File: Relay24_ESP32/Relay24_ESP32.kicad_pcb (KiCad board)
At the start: 2 copper layers, 210 x 120 mm, 163 parts, among them J1 Section 1, J10 Section 10, J11 Section 11, J12 Section 12, J13 Section 13, J14 Section 14, J15 Section 15, J16 Section 16, J17 Section 17, J18 Section 18, J19 Section 19, J2 Section 2, J20 Section 20, J21 Section 21, J22 Section 22, J23 Section 23, J24 Section 24, J25 12V IN, J26 12V ACT A (left), J27 12V ACT A (right), J28 12V ACT B (left), J29 12V ACT B (right), J3 Section 3, J30 DevKitC J2 (3V3..5V), J31 DevKitC J3 (GND..CLK), J32 HR911105A, J33 I2C, J34 Analog, J4 Section 4, J5 Section 5, J6 Section 6, J7 Section 7, J8 Section 8, J9 Section 9, K1 HF115F/012-2ZS4, K10 HF115F/012-2ZS4, K11 HF115F/012-2ZS4, K12 HF115F/012-2ZS4, K13 HF115F/012-2ZS4, K14 HF115F/012-2ZS4, K15 HF115F/012-2ZS4, K16 HF115F/012-2ZS4, K17 HF115F/012-2ZS4, K18 HF115F/012-2ZS4, K19 HF115F/012-2ZS4, K2 HF115F/012-2ZS4, K20 HF115F/012-2ZS4, K21 HF115F/012-2ZS4, K22 HF115F/012-2ZS4, K23 HF115F/012-2ZS4, K24 HF115F/012-2ZS4, K3 HF115F/012-2ZS4, K4 HF115F/012-2ZS4, K5 HF115F/012-2ZS4, K6 HF115F/012-2ZS4, K7 HF115F/012-2ZS4, K8 HF115F/012-2ZS4, K9 HF115F/012-2ZS4, U1 74HC595, U2 74HC595, U3 74HC595, U4 ULN2803A, U5 ULN2803A, U6 ULN2803A, U7 LM2596S-5.0, U8 AMS1117-3.3, U9 LAN8720A

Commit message: Relay24_ESP32: replace the LAN8720A with an RTL8201F (Economic PCBA)
JLCPCB assembles the LAN8720A (C45223) only on its Standard service,
so the Ethernet PHY is now a Realtek RTL8201F-VB-CG (C45044, QFN-32),
which is on the Economic service.

- RTL8201F runs on a 25 MHz crystal (Y1, C9006, 2x 18 pF C1647) and
  sends the 50 MHz RMII reference clock out of TXC through R30 (33 ohm)
  to GPIO0 (ETH_CLOCK_GPIO0_IN); GPIO17 is free again.
- Straps: RXDV pulled up (RMII), LED0/LED1 pulled down (PHY address 0,
  active-high LEDs). D30 shows a 10 Mbit link, D31 a 100 Mbit link.
- RSET 2.49k (C136931), PHYRSTB held low by R33 until GPIO33 is set.
- MDI pair 0 to RJ45 pins 1-2 and pair 1 to pins 3-6 (standard wiring),
  49.9 ohm terminations to 3V3 kept; new fan-out and pre-route for the
  QFN in make_pcb.py; custom schematic symbol in make_sch.py.
- router.py: the flood fill that finds existing copper of a net is now
  8-connected, so a diagonal fixed track is one piece of copper and the
  router no longer adds a wide stub next to it (clearance violation).
- make_pcb.py: RELAY24_FIXED_ONLY=1 builds only the hand-placed copper
  and runs the DRC, for quick checks.
- README, schematic, board, Gerber, BOM, CPL and views regenerated.
  Router failures 0, DRC 0 errors / 0 unconnected. Nothing built yet.

Co-Authored-By: Claude Fable 5.1 <noreply@anthropic.com>
Claude-Session: https://claude.ai/code/session_01VKEBDGHaGvWUQ7R6BJeKCx
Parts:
- removed R37: 10k, R_0603_1608Metric
- added C38: 10uF, C_0805_2012Metric, F.Cu at (55.5, 65.5)
- added Y1: 25MHz, Crystal_SMD_3225-4Pin_3.2x2.5mm, F.Cu at (68.9, 68.0)
- C34: value 1uF -> 18pF
- C35: value 10uF -> 18pF; footprint C_0805_2012Metric -> C_0603_1608Metric
- R31: value 12.1k 1% -> 2.49k 1%
- R32, R35, R36: value 10k -> 4.7k
- U9: value LAN8720A -> RTL8201F; footprint VQFN-24-1EP_4x4mm_P0.5mm_EP2.5x2.5mm_ThermalVias -> QFN-32-1EP_5x5mm_P0.5mm_EP3.45x3.45mm_ThermalVias
- moved R34 17.7 mm to (58.8, 55.3), turned to 90 degrees
- moved C35 16.5 mm to (70.8, 71.7), turned to -90 degrees
- moved R35 14.1 mm to (69.9, 56.4), turned to 90 degrees
- moved C31 13.3 mm to (71.4, 57.3), turned to 90 degrees
- moved R33 12.3 mm to (60.8, 55.3), turned to 90 degrees
- moved R43 12.0 mm to (63.4, 68.4), turned to -90 degrees
- moved R31 11.9 mm to (71.9, 63.3), turned to -90 degrees
- moved D31 7.87 mm to (63.4, 65.4), turned to 90 degrees
- moved R30 7.09 mm to (64.8, 55.3), turned to 90 degrees
- moved C32 6.48 mm to (73.5, 63.3), turned to -90 degrees
- moved C34 6.33 mm to (66.3, 68.3)
- moved R32 5.85 mm to (61.1, 63.9), turned to 0 degrees
- moved C30 5.02 mm to (66.4, 55.3), turned to 90 degrees
- moved R36 3.52 mm to (61.1, 65.6), turned to 0 degrees
- moved D30 2.70 mm to (61.1, 62.1)
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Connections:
- net LED_LNK_K renamed LED0_K
- C32 pad 1: +3V3 -> AVDD10
- C33 pad 1: VDDCR -> DVDD10
- C34 pad 1: VDDCR -> XTAL1
- C35 pad 1: +3V3 -> XTAL2
- D30 pad 2: LED_LNK -> PHY_LED0
- D31 pad 1: LED_SPD -> LED1_K
- D31 pad 2: LED_SPD_A -> PHY_LED1
- J31 pad 11: ETH_CLK -> (no net)
- J31 pad 14: (no net) -> ETH_CLK
- J32 pad 1: TXN -> MDI0P
- J32 pad 2: TXP -> MDI0N
- J32 pad 3: RXN -> MDI1P
- J32 pad 6: RXP -> MDI1N
- R30 pad 1: ETH_CLK -> ETH_REFCLK
- R30 pad 2: ETH_CLKIN -> ETH_CLK
- R31 pad 1: RBIAS -> RSET
- R32 pad 1: PHYAD0 -> GND
- R32 pad 2: GND -> PHY_LED0
- R35 pad 1: RMII_RXD0 -> PHY_RXDV
- R36 pad 1: RMII_RXD1 -> GND
- R36 pad 2: +3V3 -> PHY_LED1
- R38 pad 1: TXP -> MDI0N
- R39 pad 1: TXN -> MDI0P
- R40 pad 1: RXP -> MDI1N
- R41 pad 1: RXN -> MDI1P
- R43 pad 1: +3V3 -> LED1_K
- R43 pad 2: LED_SPD_A -> GND
- U9 pad 1: +3V3 -> RSET
- U9 pad 10: PHYAD0 -> RMII_RXD1
- U9 pad 11: RMII_CRS_DV -> (no net)
- U9 pad 12: RMII_MDIO -> (no net)
- U9 pad 13: RMII_MDC -> (no net)
- U9 pad 14: (no net) -> +3V3
- U9 pad 15: ETH_RST -> ETH_REFCLK
- U9 pad 16: RMII_TXEN -> RMII_TXD0
- U9 pad 17: RMII_TXD0 -> RMII_TXD1
- U9 pad 18: RMII_TXD1 -> (no net)
- U9 pad 19: +3V3 -> (no net)
- U9 pad 2: LED_SPD -> AVDD10
- U9 pad 20: TXN -> RMII_TXEN
- U9 pad 21: TXP -> ETH_RST
- U9 pad 22: RXN -> RMII_MDC
- U9 pad 23: RXP -> RMII_MDIO
- U9 pad 24: RBIAS -> PHY_LED0
- U9 pad 25: GND -> PHY_LED1
- U9 pad 3: LED_LNK -> MDI0P
- U9 pad 4: (no net) -> MDI0N
- U9 pad 5: ETH_CLKIN -> MDI1P
- U9 pad 6: VDDCR -> MDI1N
- U9 pad 7: RMII_RXD1 -> +3V3
- U9 pad 8: RMII_RXD0 -> PHY_RXDV
- U9 pad 9: +3V3 -> RMII_RXD0
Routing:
- net TXN: track 140.9 -> 0.00 mm, vias 1 -> 0
- net RXP: track 138.1 -> 0.00 mm, vias 1 -> 0
- net RXN: track 137.6 -> 0.00 mm, vias 1 -> 0
- net TXP: track 136.5 -> 0.00 mm, vias 1 -> 0
- net MDI0P: track 0.00 -> 131.4 mm, vias 0 -> 1
- net MDI1N: track 0.00 -> 128.1 mm, vias 0 -> 1
- net MDI1P: track 0.00 -> 126.6 mm, vias 0 -> 1
- net MDI0N: track 0.00 -> 126.0 mm, vias 0 -> 1
- net I2C_SDA: track 72.1 -> 111.8 mm, vias 1 -> 3
- net SR_Q1: track 117.8 -> 78.3 mm, vias 6 -> 2
- net GND: track 414.7 -> 452.0 mm, vias 49 -> 51
- net SR_SRCLK: track 242.8 -> 209.7 mm
- net SR_OE: track 258.7 -> 281.7 mm, vias 12 -> 9
- net ETH_CLK: track 44.1 -> 64.8 mm
- net SR_RCLK: track 200.7 -> 182.8 mm, vias 6 -> 8
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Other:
- board text added: "100M"
- board text added: "10M"
- board text removed: "LNK"
- board text removed: "SPD"

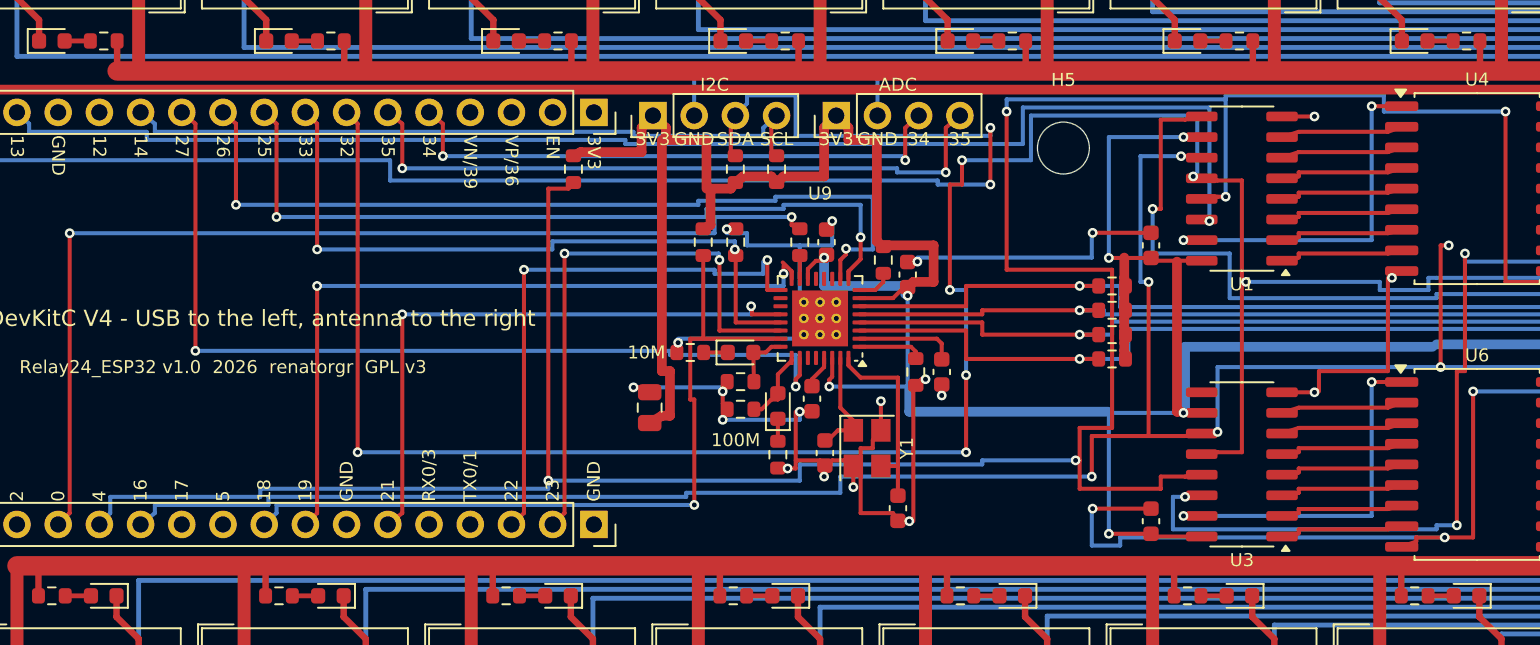
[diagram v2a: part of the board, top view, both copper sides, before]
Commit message: Relay24_ESP32: use a 5032 two-pin crystal that JLCPCB assembles normally
JLCPCB flags the 3225 four-pin crystal (C9006) as "Assembly Difficulty:
High" and warned that it may cost extra. Y1 is now the YXC X503225MSB2GI
(C112569, 25 MHz, 5.0 x 3.2 mm, two pins, CL 20 pF), which carries no
such flag.

- Load capacitors C34/C35 go from 18 pF to 33 pF (C1663, basic part)
  to match the 20 pF load capacitance.
- The crystal sits below the PHY, XTAL1 straight down from pin 31,
  XTAL2 from pin 32, each load capacitor right under its pad; the
  ground stubs and vias of the old crystal are gone.
- Schematic, board, Gerber, BOM, CPL, views and README regenerated.
  Router failures 0, DRC 0 errors / 0 unconnected.

Co-Authored-By: Claude Opus 5.5 <noreply@anthropic.com>
Claude-Session: https://claude.ai/code/session_01VKEBDGHaGvWUQ7R6BJeKCx
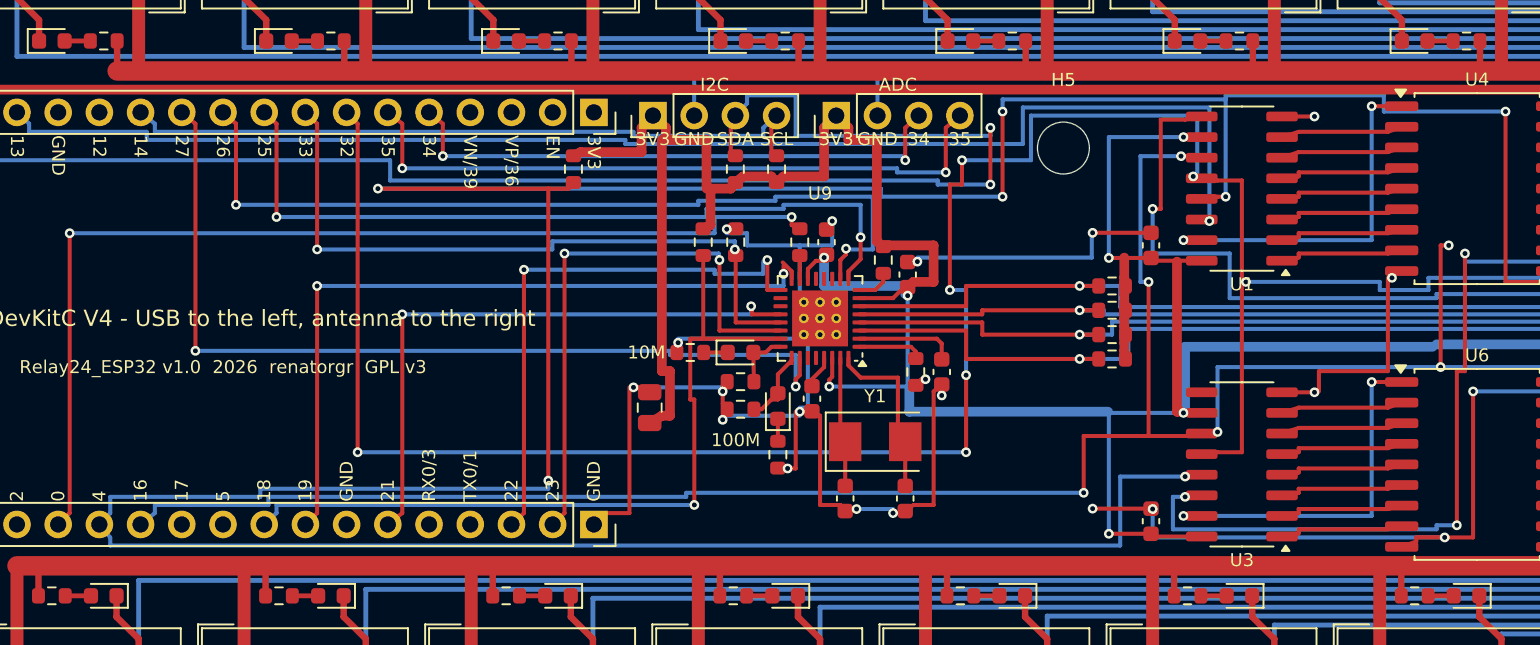
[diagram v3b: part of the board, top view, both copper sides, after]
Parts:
- C34, C35: value 18pF -> 33pF
- Y1: footprint Crystal_SMD_3225-4Pin_3.2x2.5mm -> Crystal_SMD_5032-2Pin_5.0x3.2mm
- moved C34 3.07 mm to (67.5, 71.1)
- moved C35 0.75 mm to (71.2, 71.1)
- moved Y1 0.64 mm to (69.4, 67.6), turned to 0 degrees
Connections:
- Y1 pad 2: GND -> XTAL2
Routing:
- net SR_OE: track 281.7 -> 336.0 mm, vias 9 -> 11
- net GND: track 452.0 -> 458.1 mm, vias 51 -> 50
- net XTAL2: track 12.1 -> 9.70 mm
